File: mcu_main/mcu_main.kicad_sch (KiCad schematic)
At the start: 32 parts, among them J4 4P4C_Shielded, J5 4P4C_Shielded, SW1 SW_Push_Dual, SW2 SW_Push_Dual, U1 ESP32-S3-WROOM-1, U3 SGM2212-3.3, U4 VL53L1CXV0FY1, U5 SGM2212-2.8

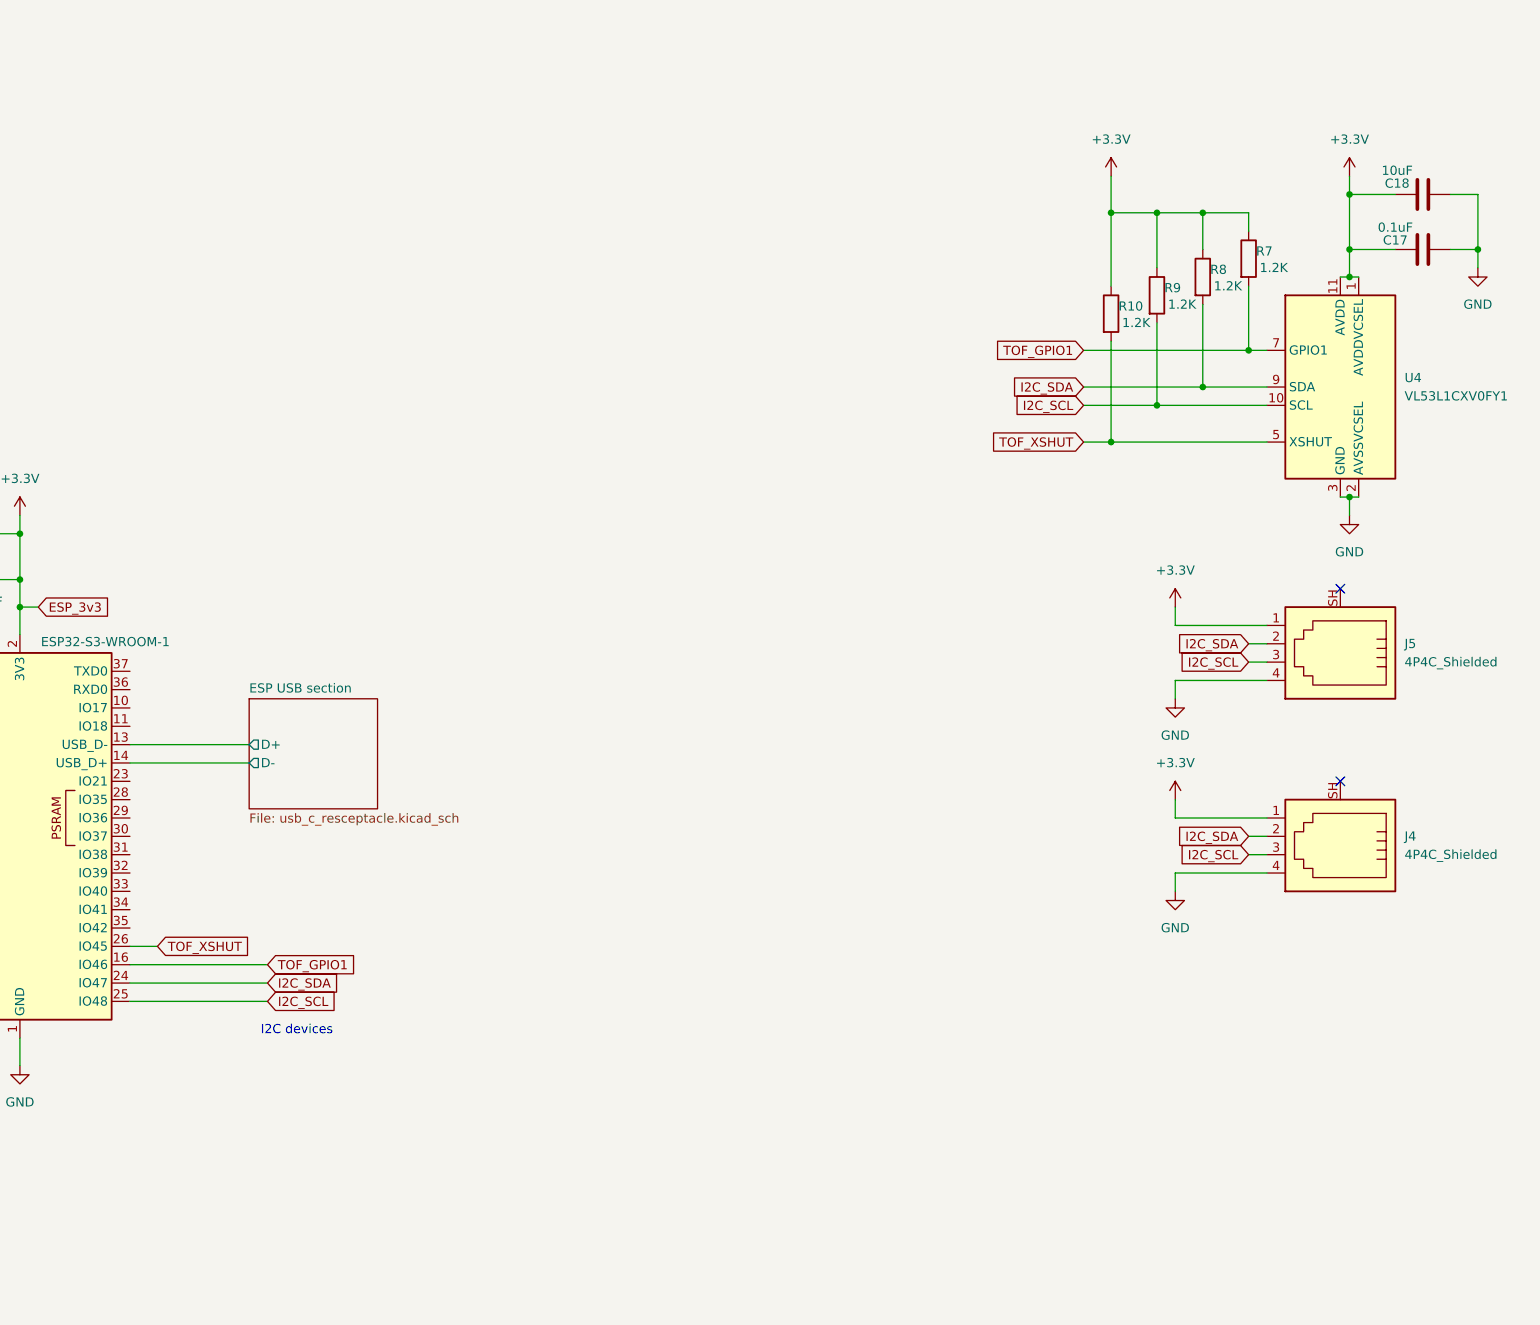
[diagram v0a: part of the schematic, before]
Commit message: Separated I2C devices into different sheets
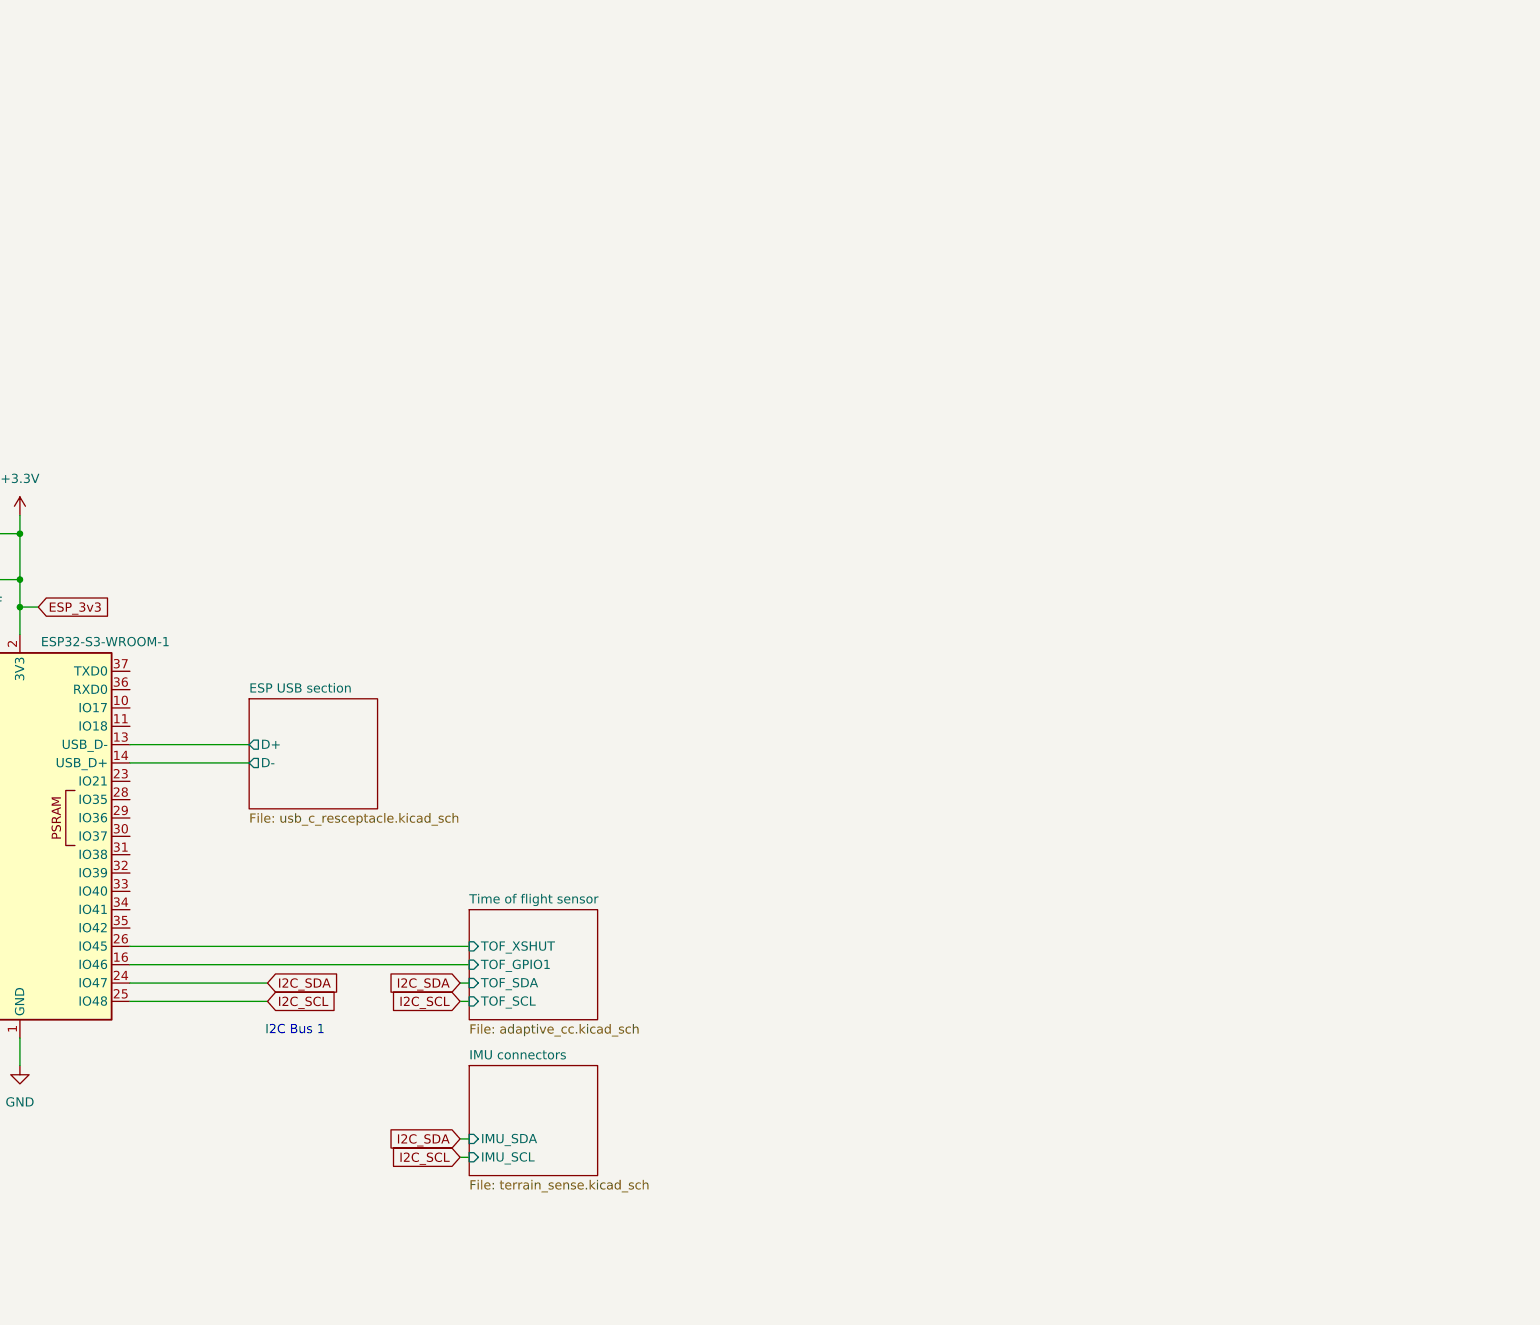
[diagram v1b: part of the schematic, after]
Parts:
- removed C17: 0.1uF, Capacitor_SMD:C_0603_1608Metric_Pad1.08x0.95mm_HandSolder, symbol Device:C
- removed C18: 10uF, Capacitor_SMD:C_0603_1608Metric_Pad1.08x0.95mm_HandSolder, symbol Device:C
- removed J4, J5: 4P4C_Shielded, Custom_footprints:JST_PH_4P_2mm_SMD, symbol Connector:4P4C_Shielded
- removed R10, R7, R8, R9: 1.2K, Resistor_SMD:R_0805_2012Metric_Pad1.20x1.40mm_HandSolder, symbol Device:R
- removed U4: VL53L1CXV0FY1, Sensor_Distance:ST_VL53L1x, symbol Sensor_Distance:VL53L1CXV0FY1
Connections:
- net TOF_GPIO1 renamed Time of flight sensor/TOF_GPIO1
- net TOF_XSHUT renamed Time of flight sensor/TOF_XSHUT
- no-connect marks 2 -> 0
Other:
- added sheet IMU connectors (terrain_sense.kicad_sch)
- added sheet Time of flight sensor (adaptive_cc.kicad_sch)
- note added: "I2C Bus 1"
- note removed: "I2C devices"

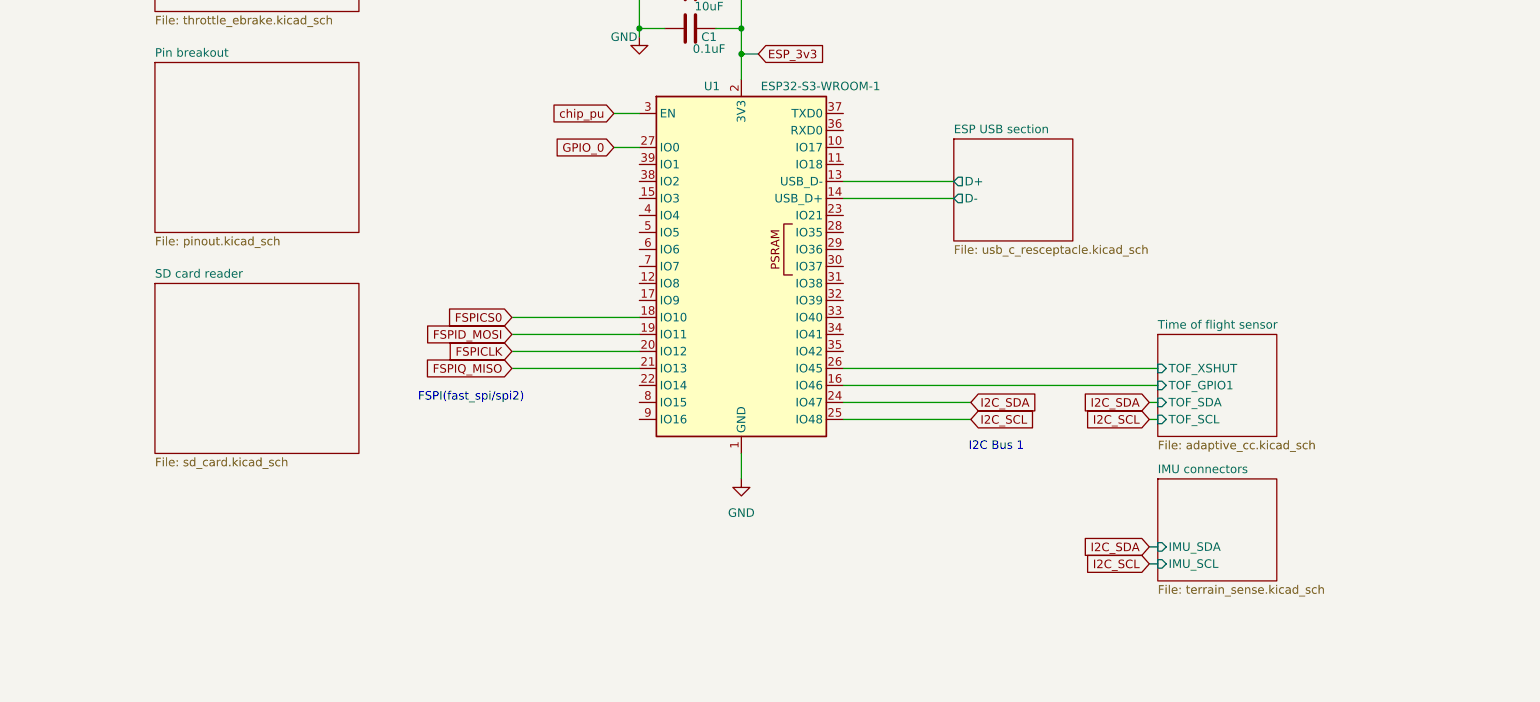
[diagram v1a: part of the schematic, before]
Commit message: SD card sheet now fits
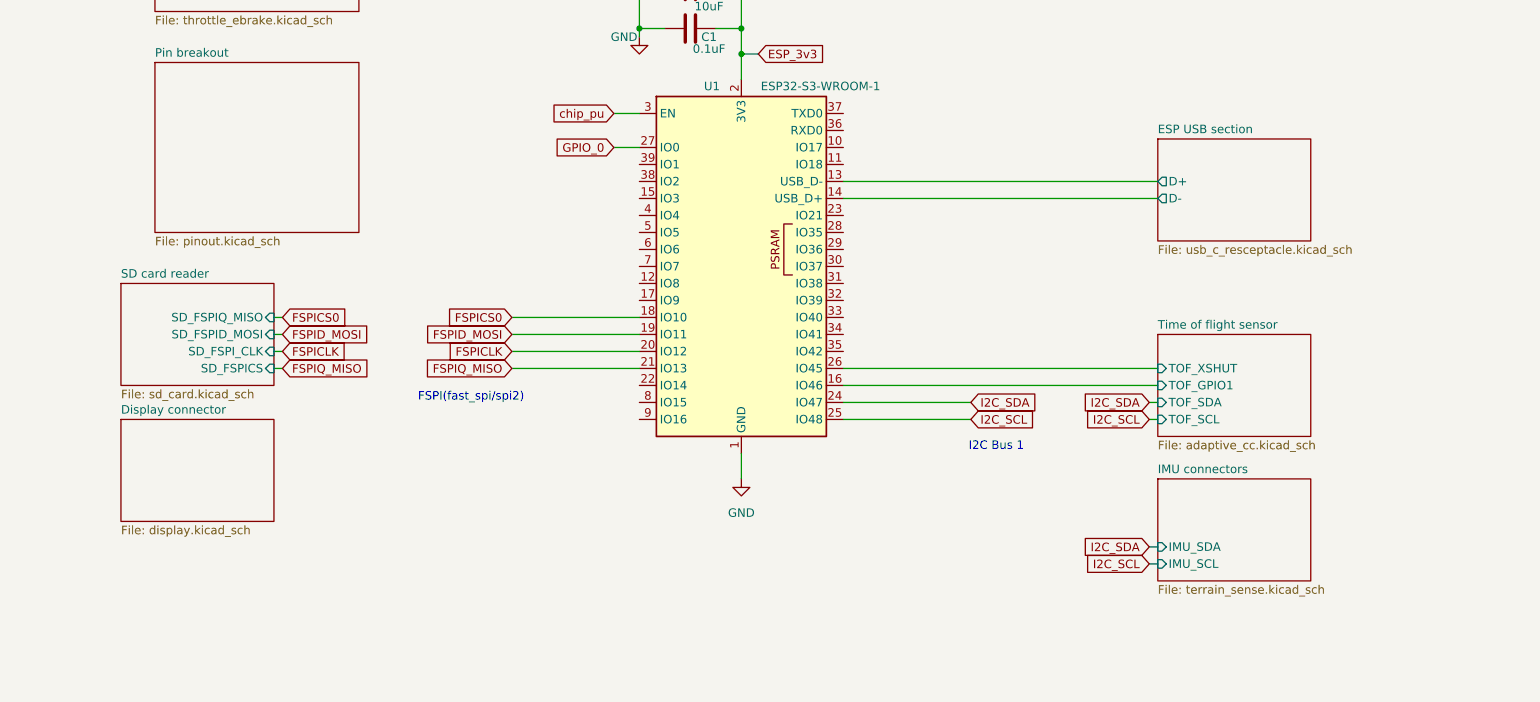
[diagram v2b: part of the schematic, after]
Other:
- added sheet Display connector (display.kicad_sch)
- sheet SD card reader ports: added SD_FSPICS, SD_FSPID_MOSI, SD_FSPIQ_MISO, SD_FSPI_CLK; removed none
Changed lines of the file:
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@@
 	(wire
 		(pts
+			(xy 72.39 162.56) (xy 71.12 162.56)
+		)
+		(stroke
+			(width 0)
+			(type default)
+		)
+	)
+	(wire
+		(pts
 			(xy 283.21 261.62) (xy 283.21 271.78)
 		)
@@
 	(wire
 		(pts
+			(xy 72.39 154.94) (xy 71.12 154.94)
+		)
+		(stroke
+			(width 0)
+			(type default)
+		)
+	)
+	(wire
+		(pts
 			(xy 220.98 252.73) (xy 220.98 246.38)
 		)
@@
 	(wire
 		(pts
+			(xy 72.39 160.02) (xy 71.12 160.02)
+		)
+		(stroke
+			(width 0)
+			(type default)
+		)
+	)
+	(wire
+		(pts
 			(xy 220.98 271.78) (xy 220.98 260.35)
 		)
@@
 	(wire
 		(pts
-			(xy 156.21 137.16) (xy 172.72 137.16)
+			(xy 156.21 137.16) (xy 203.2 137.16)
+		)
+		(stroke
+			(width 0)
+			(type default)
+		)
+	)
+	(wire
+		(pts
+			(xy 72.39 157.48) (xy 71.12 157.48)
 		)
 		(stroke
@@
 	(wire
 		(pts
-			(xy 156.21 134.62) (xy 172.72 134.62)
+			(xy 156.21 134.62) (xy 203.2 134.62)
 		)
 		(stroke
@@
 		)
 	)
+	(global_label "FSPICS0"
+		(shape input)
+		(at 72.39 154.94 0)
+		(fields_autoplaced yes)
+		(effects
+			(font
+				(size 1.27 1.27)
+			)
+			(justify left)
+		)
+		(property "Intersheetrefs" "${INTERSHEET_REFS}"
+			(at 83.2371 154.94 0)
+			(effects
+				(font
+					(size 1.27 1.27)
+				)
+				(justify left)
+				(hide yes)
+			)
+		)
+	)
 	(global_label "I2C_SCL"
 		(shape input)
@@
 		)
 	)
+	(global_label "FSPIQ_MISO"
+		(shape input)
+		(at 72.39 162.56 0)
+		(fields_autoplaced yes)
+		(effects
+			(font
+				(size 1.27 1.27)
+			)
+			(justify left)
+		)
+		(property "Intersheetrefs" "${INTERSHEET_REFS}"
+			(at 86.4424 162.56 0)
+			(effects
+				(font
+					(size 1.27 1.27)
+				)
+				(justify left)
+				(hide yes)
+			)
+		)
+	)
 	(global_label "I2C_SDA"
 		(shape input)
@@
 		)
 	)
+	(global_label "FSPICLK"
+		(shape input)
+		(at 72.39 160.02 0)
+		(fields_autoplaced yes)
+		(effects
+			(font
+				(size 1.27 1.27)
+			)
+			(justify left)
+		)
+		(property "Intersheetrefs" "${INTERSHEET_REFS}"
+			(at 83.1162 160.02 0)
+			(effects
+				(font
+					(size 1.27 1.27)
+				)
+				(justify left)
+				(hide yes)
+			)
+		)
+	)
 	(global_label "ESP_3v3"
 		(shape input)
@@
 		)
 	)
+	(global_label "FSPID_MOSI"
+		(shape input)
+		(at 72.39 157.48 0)
+		(fields_autoplaced yes)
+		(effects
+			(font
+				(size 1.27 1.27)
+			)
+			(justify left)
+		)
+		(property "Intersheetrefs" "${INTERSHEET_REFS}"
+			(at 86.3819 157.48 0)
+			(effects
+				(font
+					(size 1.27 1.27)
+				)
+				(justify left)
+				(hide yes)
+			)
+		)
+	)
 	(global_label "FSPICLK"
 		(shape input)
@@
 		(on_board yes)
 		(dnp no)
-		(fields_autoplaced yes)
 		(property "Reference" "SW1"
 			(at 40.64 251.46 0)
@@
 		(on_board yes)
 		(dnp no)
-		(fields_autoplaced yes)
 		(property "Reference" "SW2"
 			(at 87.63 251.46 0)
@@
 	)
 	(sheet
-		(at 172.72 128.27)
-		(size 17.78 15.24)
+		(at 48.26 170.18)
+		(size 22.86 15.24)
+		(exclude_from_sim no)
+		(in_bom yes)
+		(on_board yes)
+		(dnp no)
+		(fields_autoplaced yes)
+		(stroke
+			(width 0.1524)
+			(type solid)
+		)
+		(fill
+			(color 0 0 0 0.0000)
+		)
+		(property "Sheetname" "Display connector"
+			(at 48.26 169.4684 0)
+			(effects
+				(font
+					(size 1.27 1.27)
+				)
+				(justify left bottom)
+			)
+		)
+		(property "Sheetfile" "display.kicad_sch"
+			(at 48.26 186.0046 0)
+			(effects
+				(font
+					(size 1.27 1.27)
+				)
+				(justify left top)
+			)
+		)
+		(instances
+			(project "mcu_main"
+				(path "/8c1e5247-e001-4f3c-b236-a22b9c821843"
+					(page "8")
+				)
+			)
+		)
+	)
+	(sheet
+		(at 203.2 128.27)
+		(size 22.86 15.24)
 		(exclude_from_sim no)
 		(in_bom yes)
@@
 		)
 		(property "Sheetname" "ESP USB section"
-			(at 172.72 127.5584 0)
+			(at 203.2 127.5584 0)
 			(effects
 				(font
@@
 		)
 		(property "Sheetfile" "usb_c_resceptacle.kicad_sch"
-			(at 172.72 144.0946 0)
+			(at 203.2 144.0946 0)
 			(effects
 				(font
@@
 		)
 		(pin "D+" output
-			(at 172.72 134.62 180)
+			(at 203.2 134.62 180)
 			(effects
 				(font
@@
 		)
 		(pin "D-" output
-			(at 172.72 137.16 180)
+			(at 203.2 137.16 180)
 			(effects
 				(font
@@
 	)
 	(sheet
-		(at 53.34 149.86)
-		(size 30.48 25.4)
+		(at 48.26 149.86)
+		(size 22.86 15.2399)
 		(exclude_from_sim no)
 		(in_bom yes)
@@
 		)
 		(property "Sheetname" "SD card reader"
-			(at 53.34 149.1484 0)
+			(at 48.26 149.1484 0)
 			(effects
 				(font
@@
 		)
 		(property "Sheetfile" "sd_card.kicad_sch"
-			(at 53.34 175.8446 0)
+			(at 48.26 165.6845 0)
 			(effects
 				(font
@@
 			)
 		)
+		(pin "SD_FSPID_MOSI" input
+			(at 71.12 157.48 0)
+			(effects
+				(font
+					(size 1.27 1.27)
+				)
+				(justify right)
+			)
+		)
+		(pin "SD_FSPI_CLK" input
+			(at 71.12 160.02 0)
+			(effects
+				(font
+					(size 1.27 1.27)
+				)
+				(justify right)
+			)
+		)
+		(pin "SD_FSPICS" input
+			(at 71.12 162.56 0)
+			(effects
+				(font
+					(size 1.27 1.27)
+				)
+				(justify right)
+			)
+		)
+		(pin "SD_FSPIQ_MISO" input
+			(at 71.12 154.94 0)
+			(effects
+				(font
+					(size 1.27 1.27)
+				)
+				(justify right)
+			)
+		)
 		(instances
 			(project "mcu_main"
@@
 	(sheet
 		(at 203.2 157.48)
-		(size 17.78 15.24)
+		(size 22.86 15.24)
 		(exclude_from_sim no)
 		(in_bom yes)
@@
 	(sheet
 		(at 203.2 179.07)
-		(size 17.78 15.24)
+		(size 22.86 15.24)
 		(exclude_from_sim no)
 		(in_bom yes)
